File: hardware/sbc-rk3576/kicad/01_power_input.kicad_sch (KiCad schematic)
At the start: 12 parts, among them J101 USB-C PWR/OTG

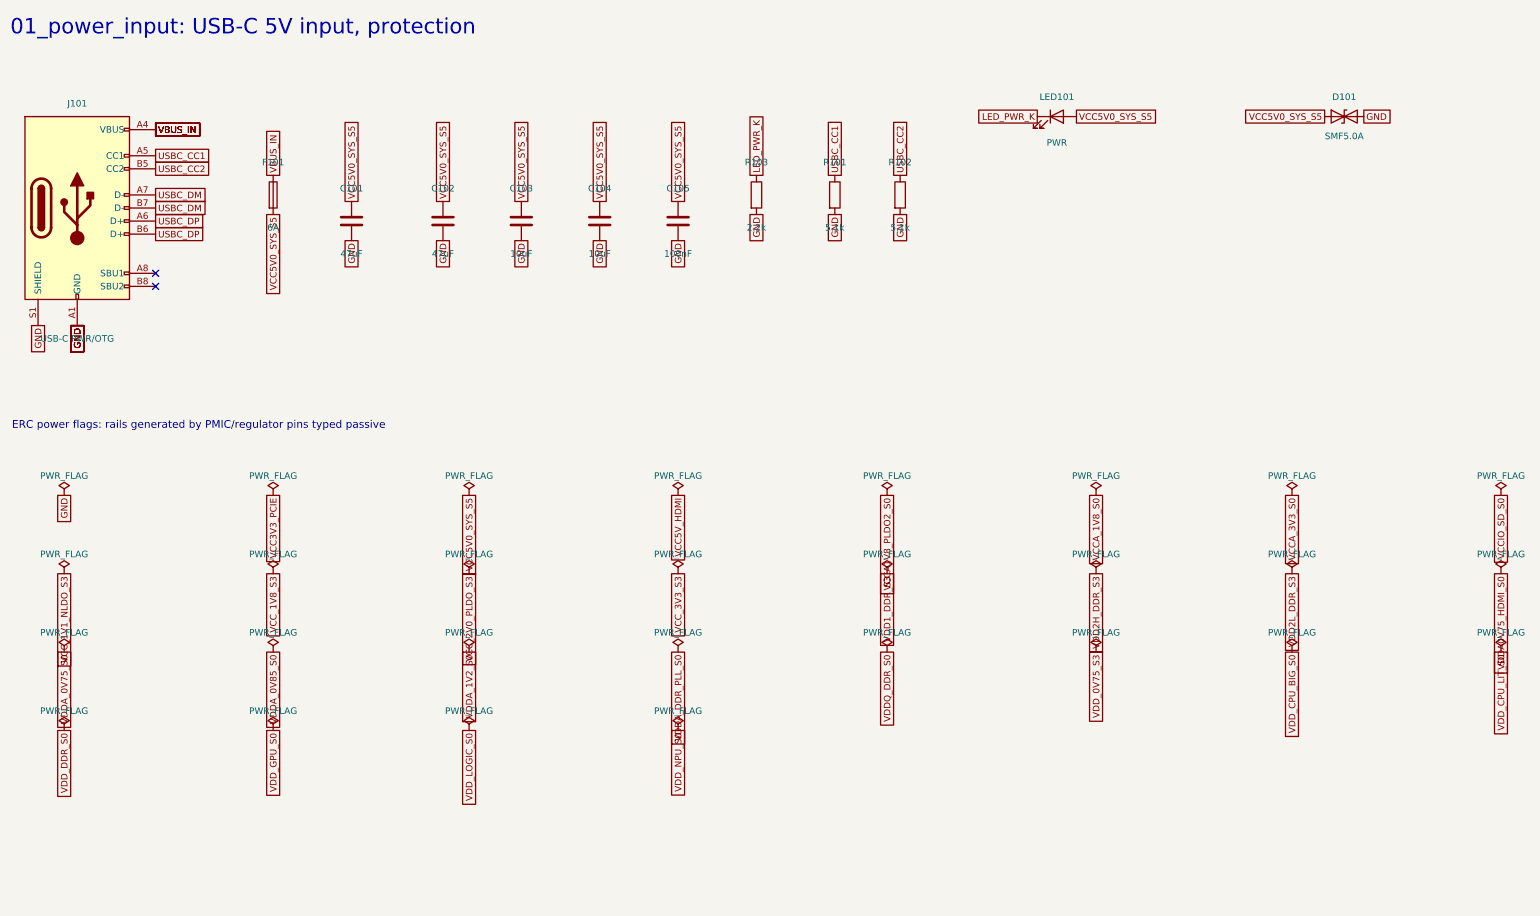
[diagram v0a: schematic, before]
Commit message: hardware: add GbE, USB hub + 2x USB-A, Wi-Fi5/BT; real RK3576 land pattern; 100x72 board
- RK3576 footprint from LCSC C42388007 (all 698 ball IDs verified against the
  datasheet) replaces the placeholder.
- RTL8211F-CG RGMII PHY + HR911130C MagJack, FE1.1s 4-port hub (pinout per
  Terminus datasheet), stacked dual USB-A, BL-M8821CU1 Wi-Fi 5/BT 4.2 + u.FL.
- LCSC footprints get pad-derived courtyards; RJ45 pegs become NPTH.
- ERC 0/0, DRC 0 violations, parity 0 (placement stage).

Co-Authored-By: Claude Opus 5.5 <noreply@anthropic.com>
Claude-Session: https://claude.ai/code/session_01DP7VBm9fUdwhcDWq3gWKJ6
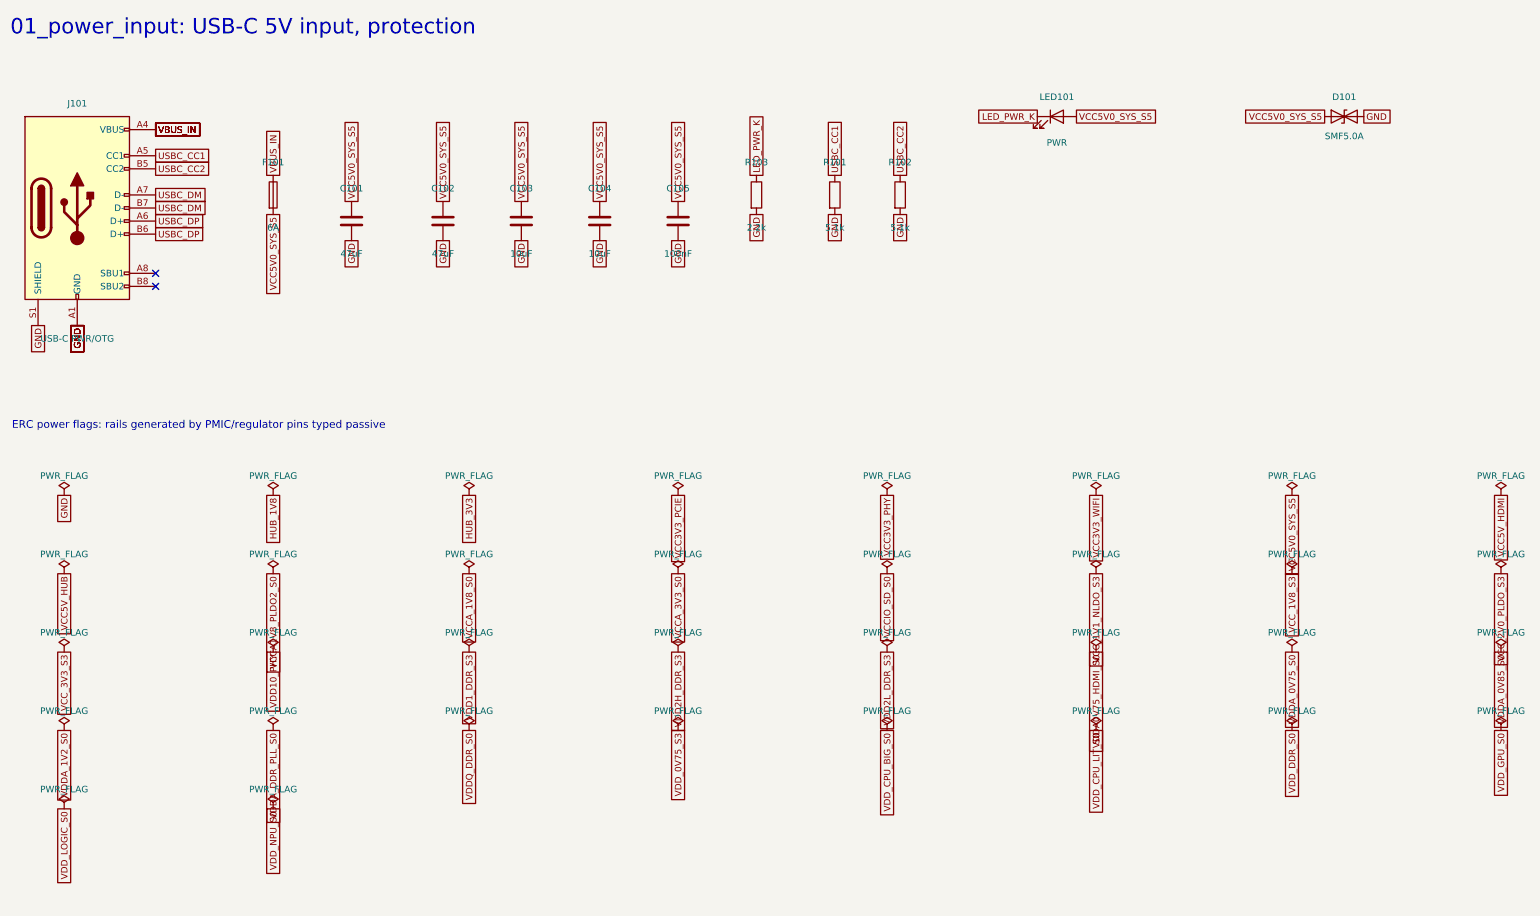
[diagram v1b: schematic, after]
